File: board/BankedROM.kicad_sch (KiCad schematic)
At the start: 16 parts, among them U30 SST39SF040, U31 SST39SF040, U32 SST39SF040, U33 SST39SF040, U34 SST39SF040, U35 SST39SF040, U36 SST39SF040, U37 SST39SF040

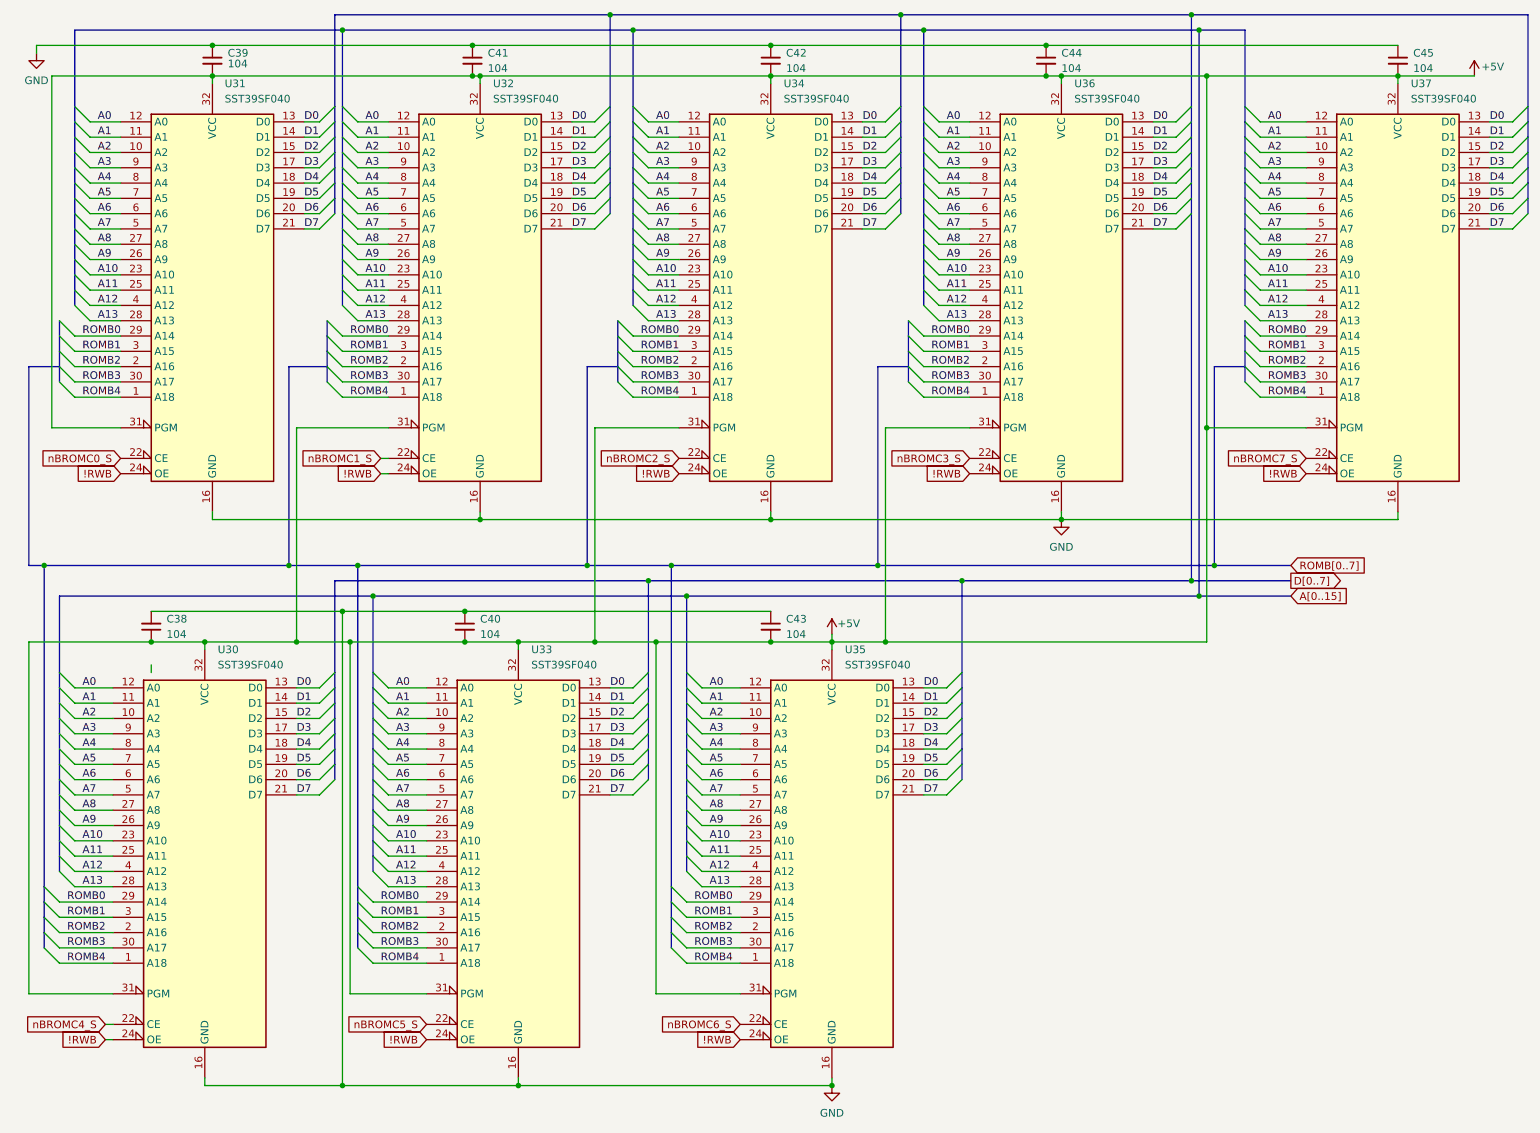
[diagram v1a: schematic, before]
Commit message: V2.0 updates and new hydra breakout and counter cards.
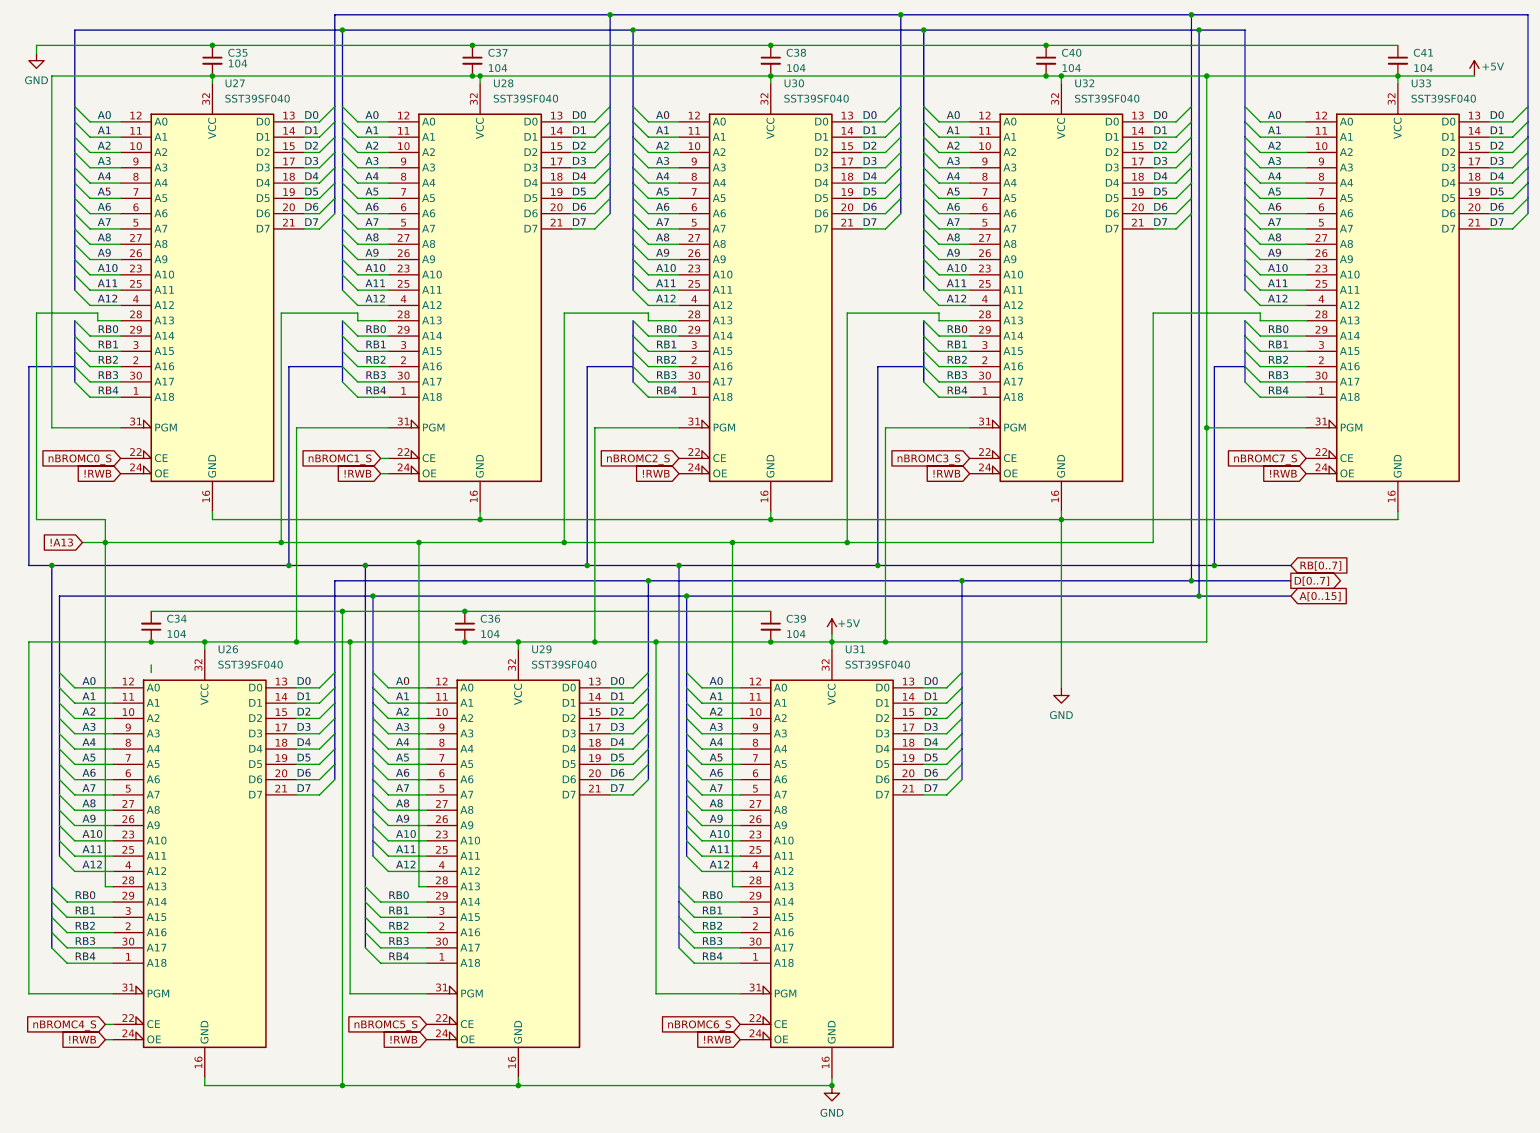
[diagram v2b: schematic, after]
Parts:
- renumbered C38 to C34, C39 to C35, C40 to C36, C41 to C37, C42 to C38, C43 to C39, C44 to C40, C45 to C41, U30 to U26, U31 to U27, U32 to U28, U33 to U29, U34 to U30, U35 to U31, U36 to U32, U37 to U33
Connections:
- net A13 renamed !A13
- net ROMB0 renamed RB0
- net ROMB1 renamed RB1
- net ROMB2 renamed RB2
- net ROMB3 renamed RB3
- net ROMB4 renamed RB4
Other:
- title: Shared ROM Banks -> ZeroPage $00/$01 Mirror Memory and RAM/ROM Bank Logic
